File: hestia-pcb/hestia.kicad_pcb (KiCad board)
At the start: 4 copper layers, 90.2 x 95.9 mm, 181 parts, among them J1 Serial Connector, J12 B2B-ZR, J13 B2B-ZR, J14 B2B-ZR, J15 B2B-ZR, J16 B2B-ZR, J2 i2c connector, J3 ESQ-126-39-G-D, J4 ESQ-126-39-G-D, J5 VREF+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

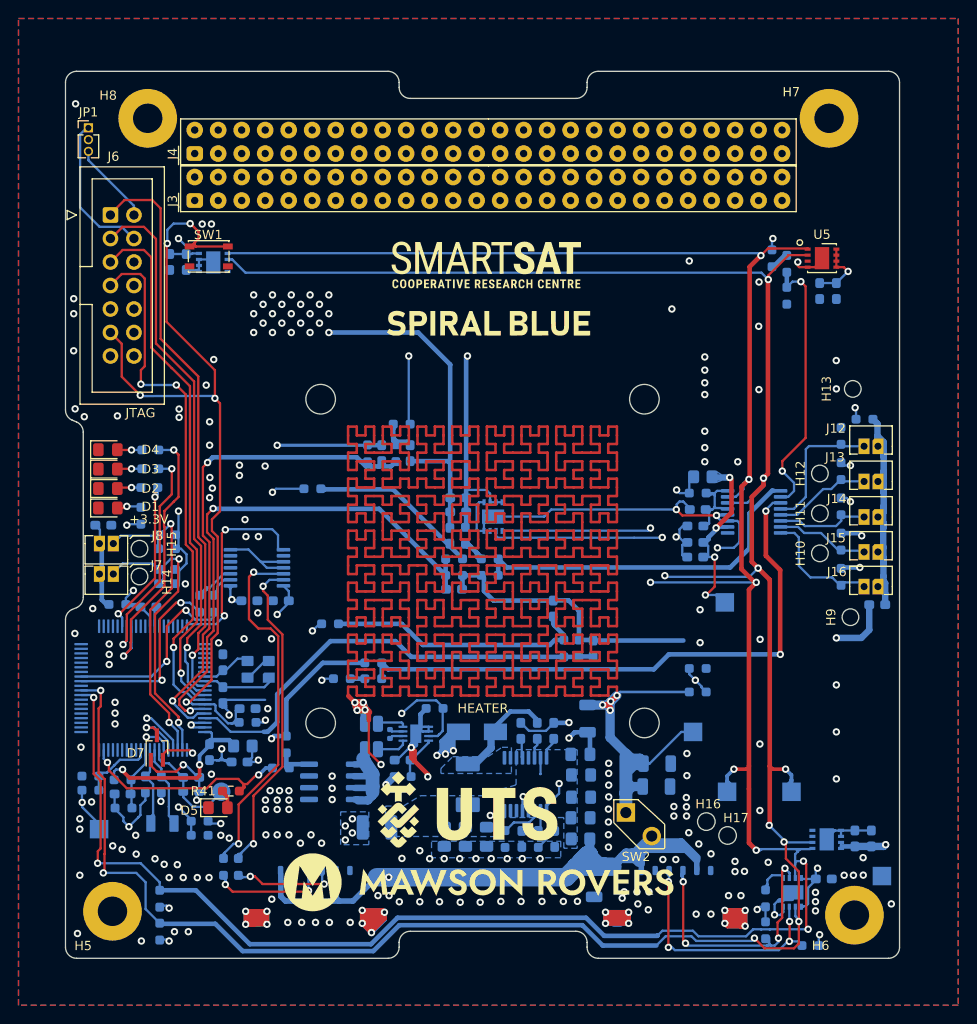
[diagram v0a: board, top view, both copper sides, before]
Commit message: Added pcb trace to C13 to satisfy minimum-of-2 thermal relief spokes DRC violation. Moved U3 designator for better clarity. Added pcb trace to U3 pin 9 to satisfy minimum-of-2 thermal relief spokes DRC violation. Added pcb trace to U3 pin 12 to satisfy minimum-of-2 thermal relief spokes DRC violation. Added pcb trace to U3 pin 11 to satisfy minimum-of-2 thermal relief spokes DRC violation. Added pcb trace to C50 pin 2 to satisfy minimum-of-2 thermal relief spokes DRC violation. Added pcb trace to C41 pin 2 to satisfy minimum-of-2 thermal relief spokes DRC violation. Added pcb trace to U4 pin 4 to satisfy minimum-of-2 thermal relief spokes DRC violation. Added pcb trace to U6 pin 4 to satisfy minimum-of-2 thermal relief spokes DRC violation. Added pcb trace to U9 pin 4 to satisfy minimum-of-2 thermal relief spokes DRC violation.
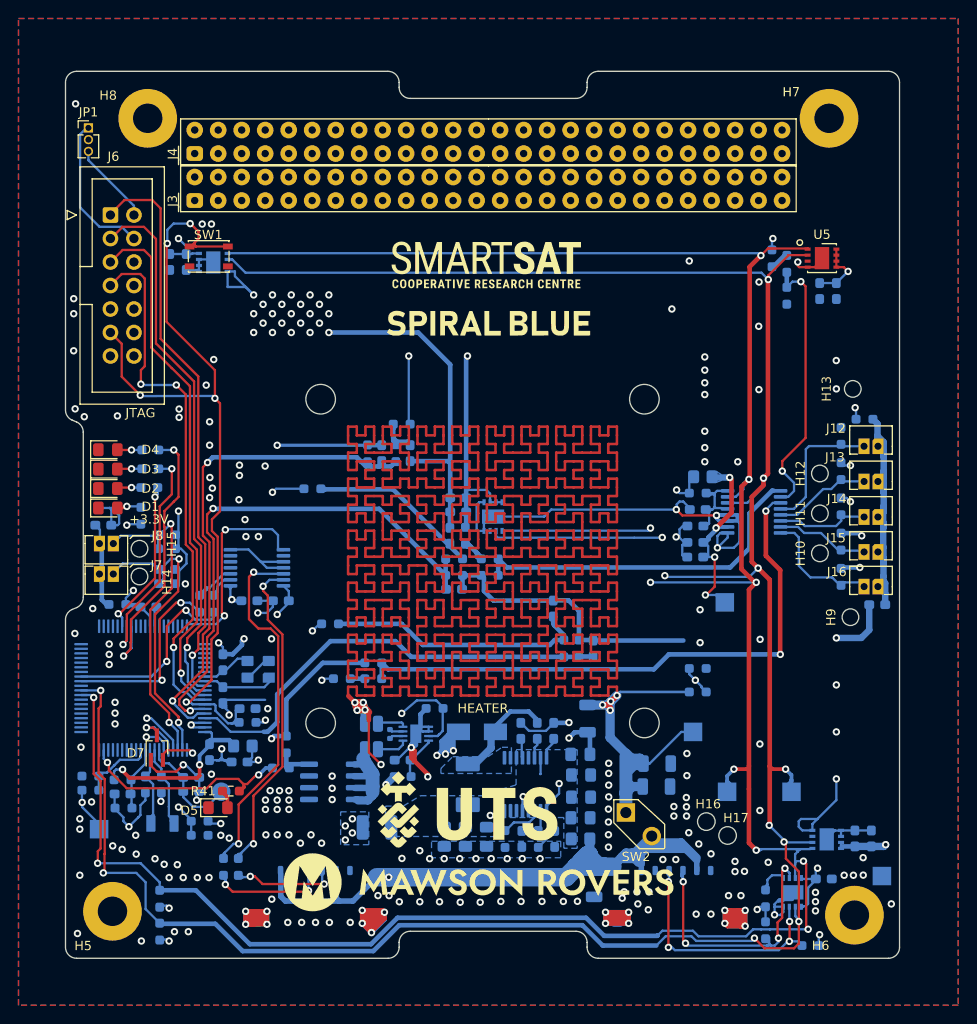
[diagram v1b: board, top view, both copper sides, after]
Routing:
- net GND: track 285.0 -> 329.7 mm

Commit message: Updated TP4 TestPoint footprint from newer Kicad 7 footprints library due to DRC warning re: mismatch of part in design vs part in referenced library. Updated R26 NetTie footprint from newer Kicad 7 footprints library due to DRC warning re: mismatch of part in design vs part in referenced library. Updated D6 footprint from newer Kicad 7 footprints library due to DRC warning re: mismatch of part in design vs part in referenced library. Updated H5 footprint from Hestia footprints library due to DRC warning re: mismatch of part in design vs part in referenced library - not sure why there is a difference from the library - no difference was observed after update. Added pcb traces to R20 pin 1 to satisfy minimum-of-2 thermal relief spokes DRC violation. Todo: logos need to be rereferenced back to hestia library footprints or added. two logos don't seem to have libraries
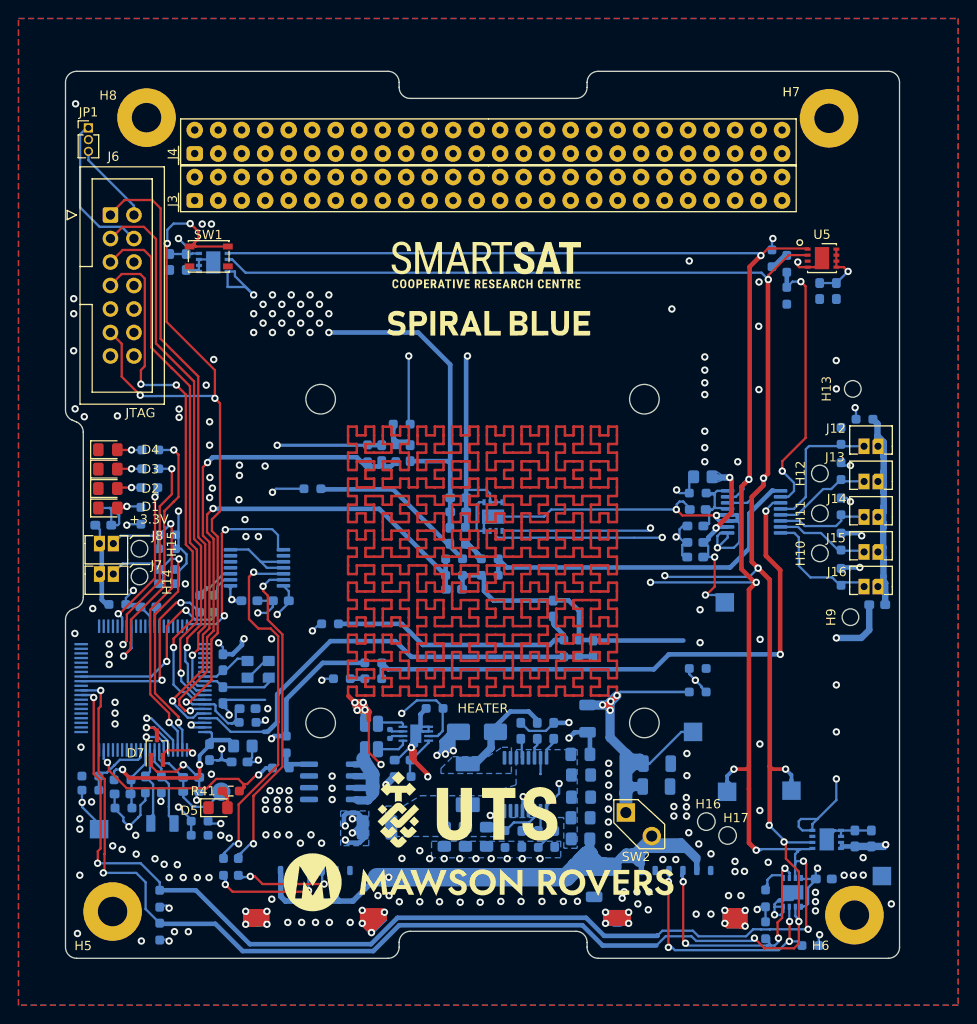
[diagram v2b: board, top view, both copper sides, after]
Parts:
- LOGO1: renamed from G***; value LOGO -> MAWSON ROVERS LOGO
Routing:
- net +3.3V: track 115.0 -> 127.5 mm

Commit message: Added four new footprints to hestia library: SpiralBlue Logo, SmartSatCRCLogo, a second different size Mawson Rovers Logo with a suffix 2, A second UTS logo with suffix 2- it wasn't clear if it was a different size but Kicad did not register the existing UTS logo footprint library as being linked to the logo footprint on the PCB. The PCB was then updated with the new footprints from the hestia library footprints. All DRC warnings and errors are now currently resolved. ToDo: review VCC and ground traces exiting pico lock connectors.
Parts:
- LOGO1: value MAWSON ROVERS LOGO -> MAWSON ROVERS; footprint LOGO -> Hestia:Logo_Mawson_Rovers_2
- LOGO2: renamed from G***; value LOGO -> UTS; footprint LOGO -> Hestia:Logo_UTS_2
- LOGO3: renamed from G***; value LOGO -> SMARTSATCRC; footprint LOGO -> Hestia:Logo_SmartSatCRC
- LOGO4: renamed from G***; value LOGO -> SPIRALBLUE; footprint LOGO -> Hestia:Logo_SpiralBlue
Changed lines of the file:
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@@
     )
   )
-  (footprint "LOGO" (layer "F.Cu")
+  (footprint "Hestia:Logo_SmartSatCRC" (layer "F.Cu")
     (at 147.0914 81.9811)
     (attr board_only exclude_from_pos_files exclude_from_bom)
-    (fp_text reference "G***" (at -5.588 -38.608) (layer "F.SilkS") hide
+    (fp_text reference "LOGO3" (at -5.588 -38.608) (layer "F.SilkS") hide
         (effects (font (size 1.524 1.524) (thickness 0.3)))
     )
-    (fp_text value "LOGO" (at 0.75 0) (layer "F.SilkS") hide
+    (fp_text value "SMARTSATCRC" (at 0.75 0) (layer "F.SilkS") hide
         (effects (font (size 1.524 1.524) (thickness 0.3)))
     )
@@
       (stroke (width 0) (type solid)) (fill solid) (layer "F.SilkS"))
   )
-  (footprint "LOGO" (layer "F.Cu")
+  (footprint "Hestia:Logo_UTS_2" (layer "F.Cu")
     (at 145.0594 140.9091)
     (attr board_only exclude_from_pos_files exclude_from_bom)
-    (fp_text reference "G***" (at 3.048 -24.892) (layer "F.SilkS") hide
+    (fp_text reference "LOGO2" (at 3.048 -24.892) (layer "F.SilkS") hide
         (effects (font (size 1.524 1.524) (thickness 0.3)))
     )
-    (fp_text value "LOGO" (at 0.75 0) (layer "F.SilkS") hide
+    (fp_text value "UTS" (at 0.75 0) (layer "F.SilkS") hide
         (effects (font (size 1.524 1.524) (thickness 0.3)))
     )
@@
       (net 224 "A5_b") (pinfunction "2") (pintype "input"))
   )
-  (footprint "LOGO" (layer "F.Cu")
+  (footprint "Hestia:Logo_SpiralBlue" (layer "F.Cu")
     (at 147.3454 88.3311)
     (attr board_only exclude_from_pos_files exclude_from_bom)
-    (fp_text reference "G***" (at 0 10.668) (layer "F.SilkS") hide
+    (fp_text reference "LOGO4" (at 0 10.668) (layer "F.SilkS") hide
         (effects (font (size 1.524 1.524) (thickness 0.3)))
     )
-    (fp_text value "LOGO" (at 0.75 0) (layer "F.SilkS") hide
+    (fp_text value "SPIRALBLUE" (at 0.75 0) (layer "F.SilkS") hide
         (effects (font (size 1.524 1.524) (thickness 0.3)))
     )
@@
       (net 65 "unconnected-(J3-Pad52)") (pinfunction "52") (pintype "unspecified+no_connect"))
   )
-  (footprint "LOGO" (layer "F.Cu")
+  (footprint "Hestia:Logo_Mawson_Rovers_2" (layer "F.Cu")
     (at 146.972851 148.782205)
     (attr board_only exclude_from_pos_files exclude_from_bom)
@@
         (effects (font (size 1.524 1.524) (thickness 0.3)))
     )
-    (fp_text value "MAWSON ROVERS LOGO" (at 0.75 0) (layer "F.SilkS") hide
+    (fp_text value "MAWSON ROVERS" (at 0.75 0) (layer "F.SilkS") hide
         (effects (font (size 1.524 1.524) (thickness 0.3)))
     )

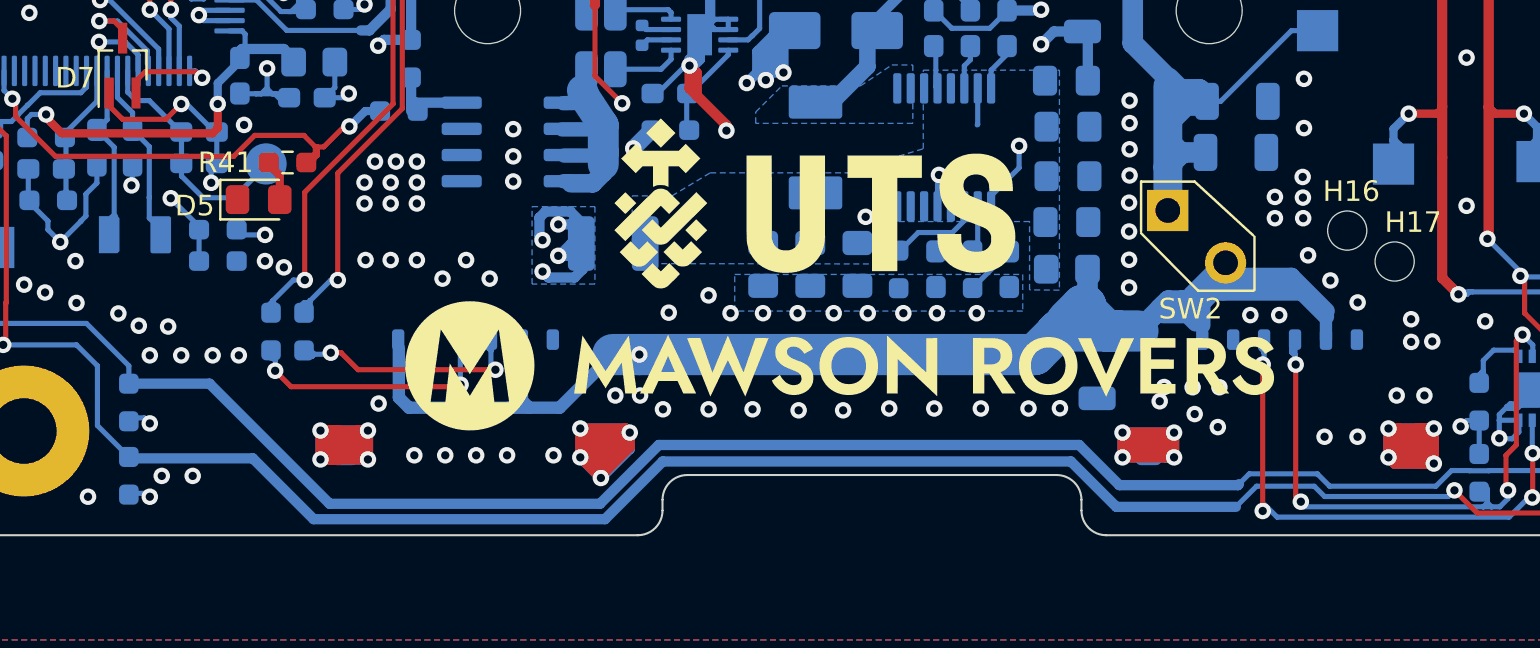
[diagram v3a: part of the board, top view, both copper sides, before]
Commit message: Added extra PCB trace on C8 pin2 for extra ground current path. Shifted VCC via at x=136.56,y=148.12 slightly to allow extra connection path on VCC internal plane. Widen VCC path at J1 and J2 with pcb traces and polygon area fill. Added GND traces at J1 and J2 for better ground connection at pico lock connectors. Shifted SCL_3.3V and SDA_3.3V near R21 to relieve GND plane choke point and added a GND via between I2c signals. Move H6 designator back on to PCB. DRC resolved. ToDo: Inspect designator placements
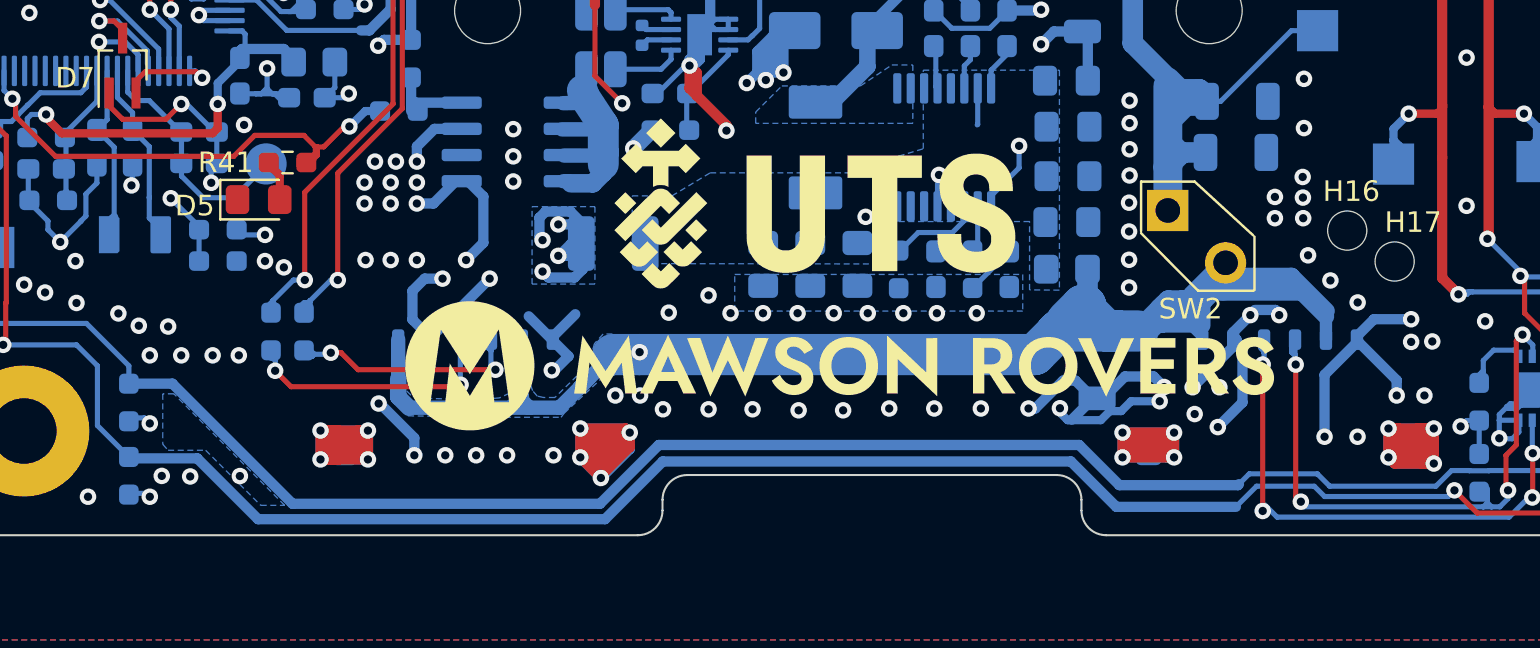
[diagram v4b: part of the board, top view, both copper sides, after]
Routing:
- net GND: track 329.7 -> 396.3 mm, vias 225 -> 227
- net VCC: track 109.7 -> 115.3 mm
- added copper zone on B.Cu, net VCC
